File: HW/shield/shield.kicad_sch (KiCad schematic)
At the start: 82 parts, among them J1 TRG, J2 E-STOP, J3 UART, J4 IO, J5 LDP-C BOB, J6 VIN, J7 BREAK, Q1 BSS138, Q2 BSS138, Q3 BSS138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

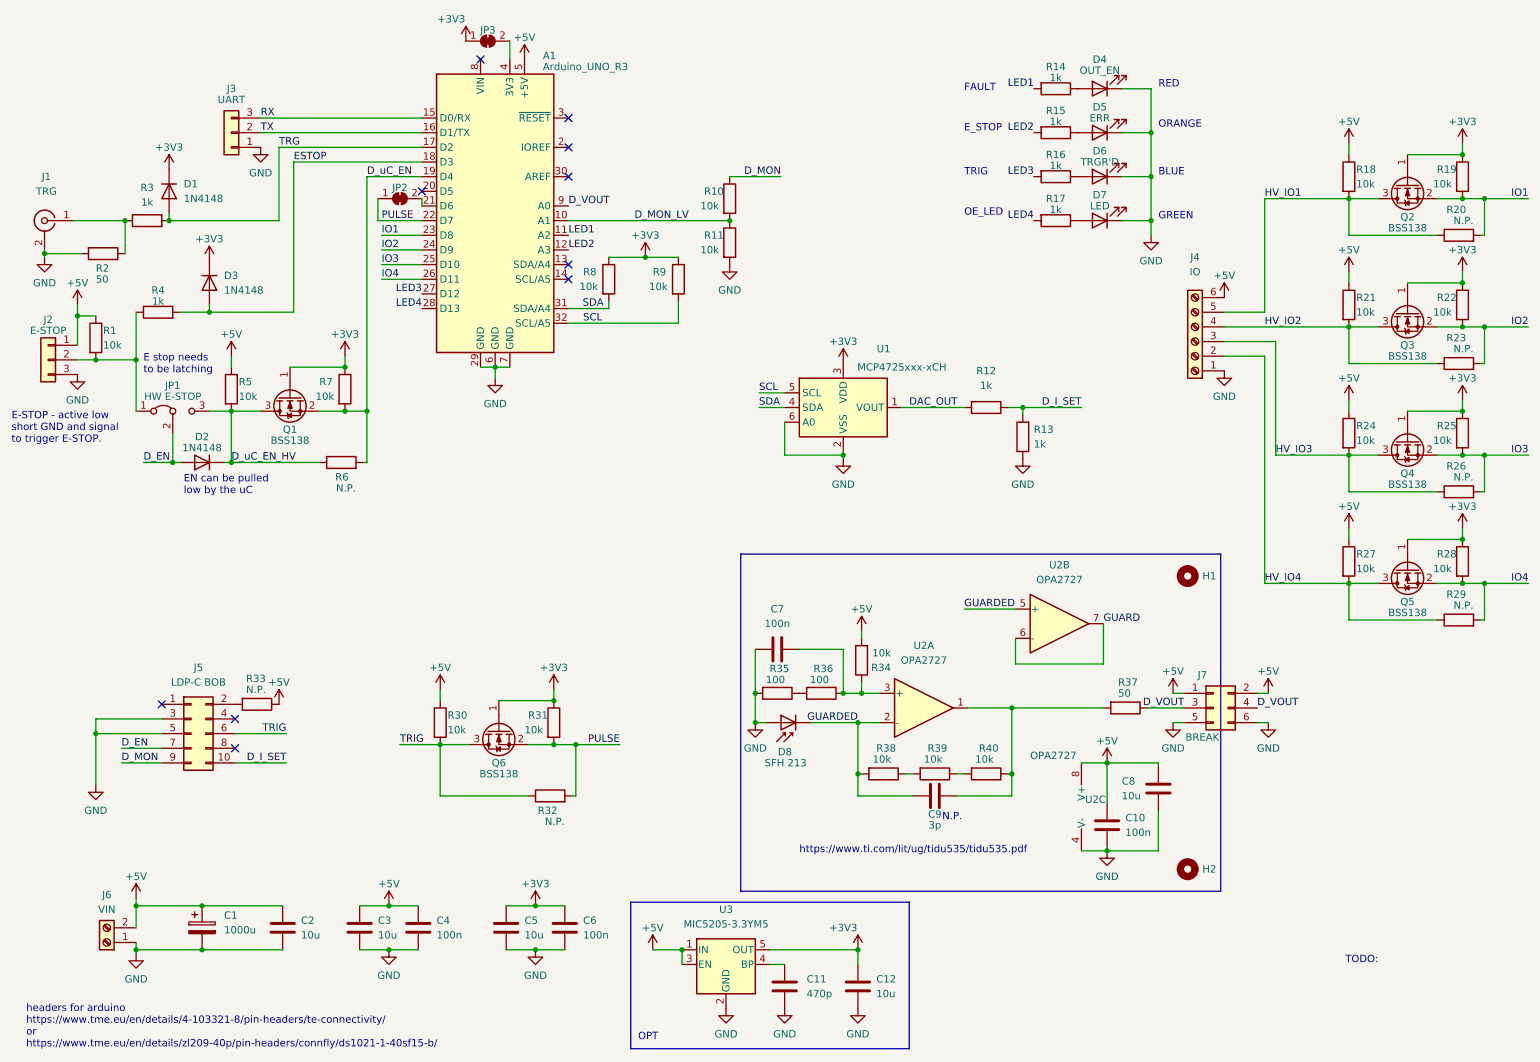
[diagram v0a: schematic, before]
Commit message: added screenshots, adjusted schematics for better layout
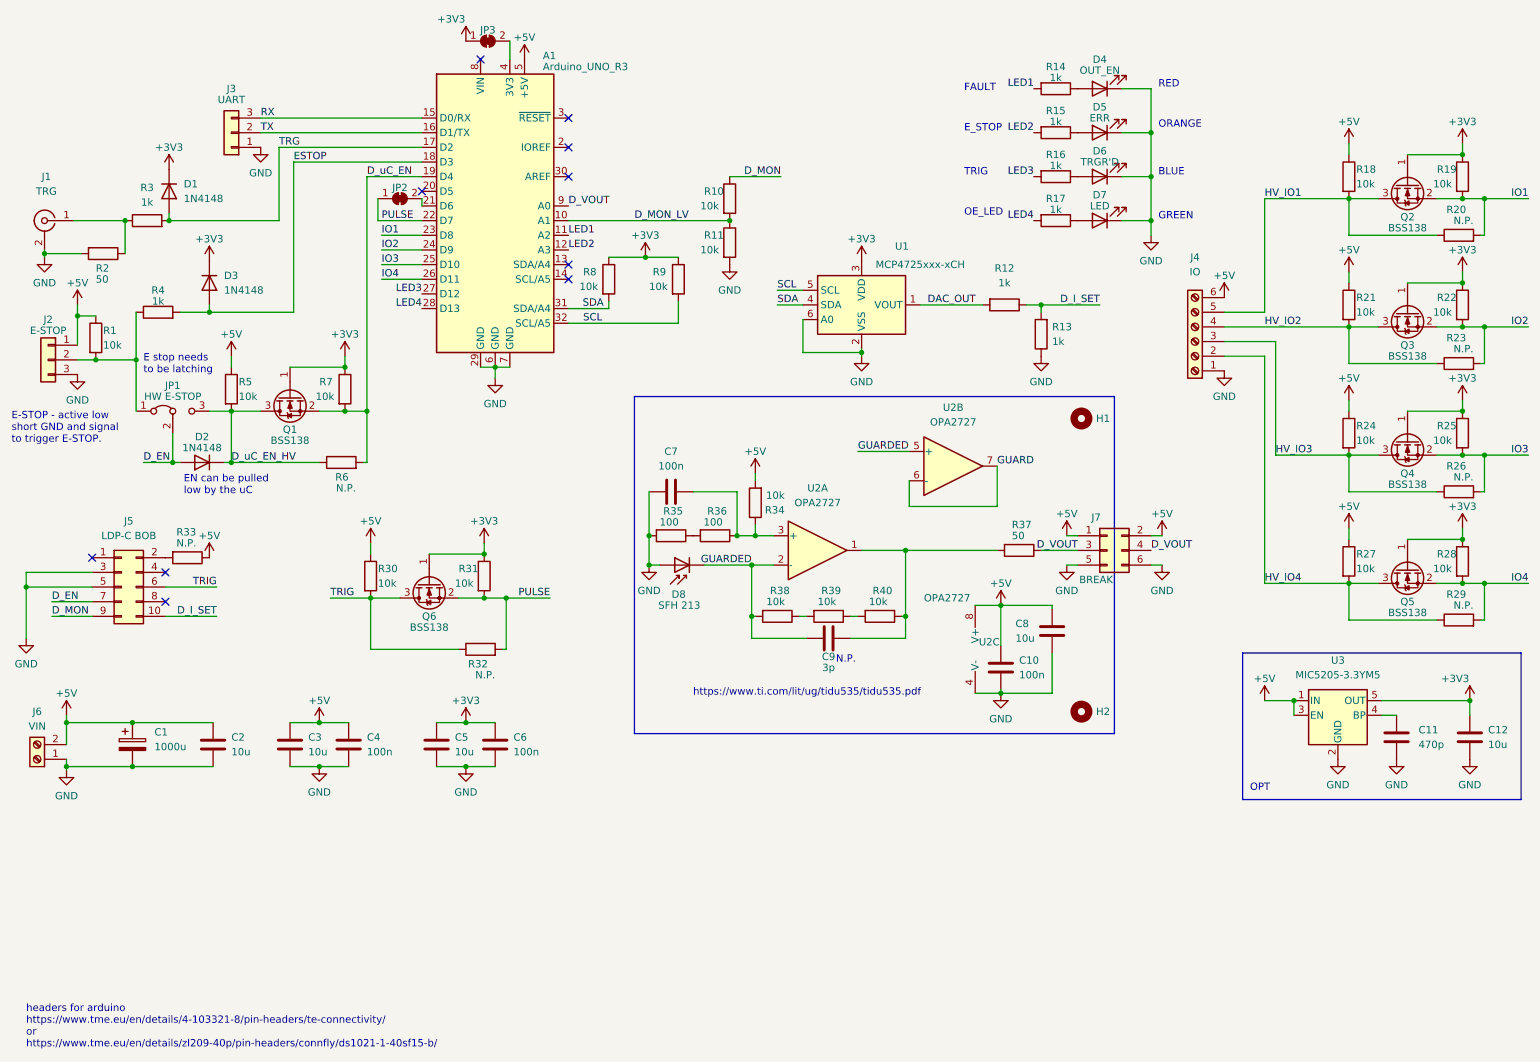
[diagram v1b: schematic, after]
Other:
- note removed: "TODO:"
- moved on the sheet: C1, C10, C11, C12, C2, C3, C4, C5, C6, C7, C8, C9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
